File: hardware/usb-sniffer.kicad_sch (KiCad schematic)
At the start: 40 parts, among them IC1 LCMXO2-2000HC, IC2 MIC5504-3.3v, J1 USB-C, J2 USB-C, J3 USB-A, J4 IN, J5 GND

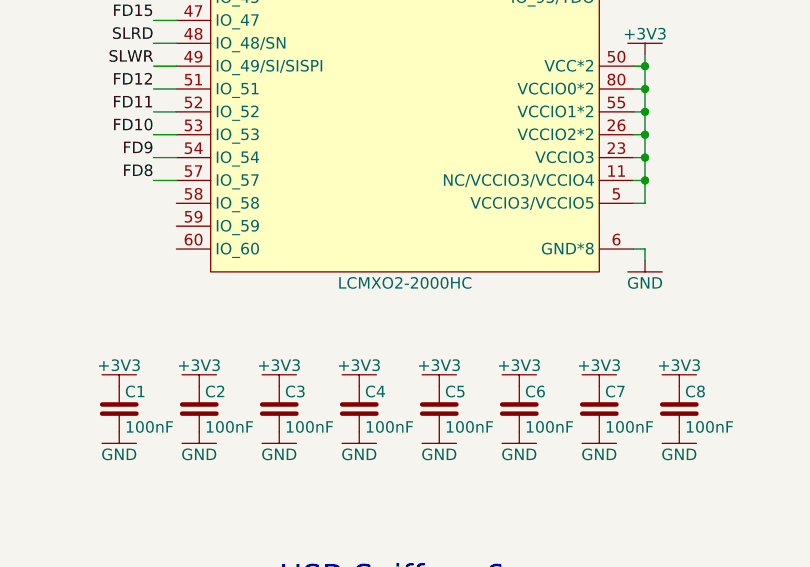
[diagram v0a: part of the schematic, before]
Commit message: Added EEPROM part name
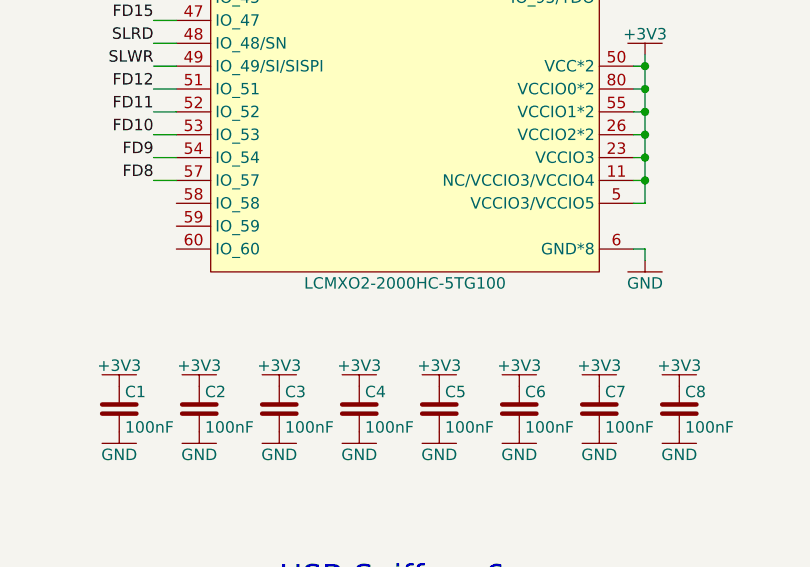
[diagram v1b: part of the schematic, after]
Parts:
- IC1: value LCMXO2-2000HC -> LCMXO2-2000HC-5TG100
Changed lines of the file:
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@@
   (paper "USLetter")
   (title_block
-    (date "2023-05-06")
+    (date "2023-06-16")
     (rev "6")
   )
@@
       (effects (font (size 1.27 1.27)))
     )
-    (property "Value" "LCMXO2-2000HC" (at 146.05 149.86 0)
+    (property "Value" "LCMXO2-2000HC-5TG100" (at 146.05 149.86 0)
       (effects (font (size 1.27 1.27)))
     )

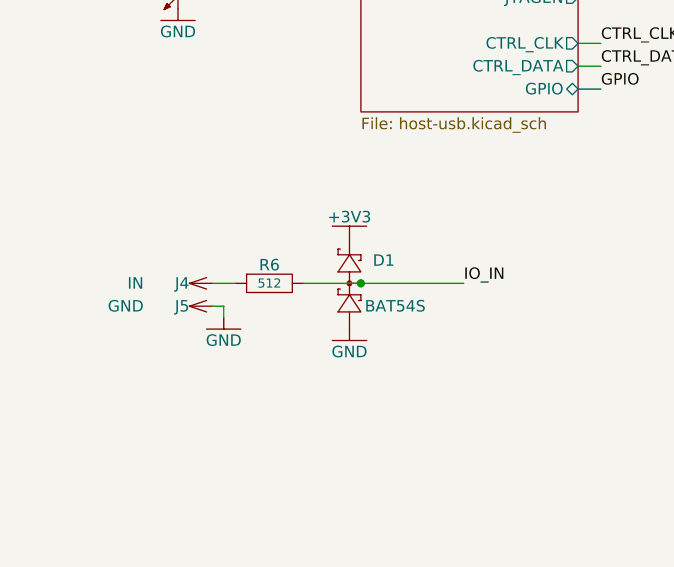
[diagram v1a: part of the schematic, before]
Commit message: Fixed resistor value
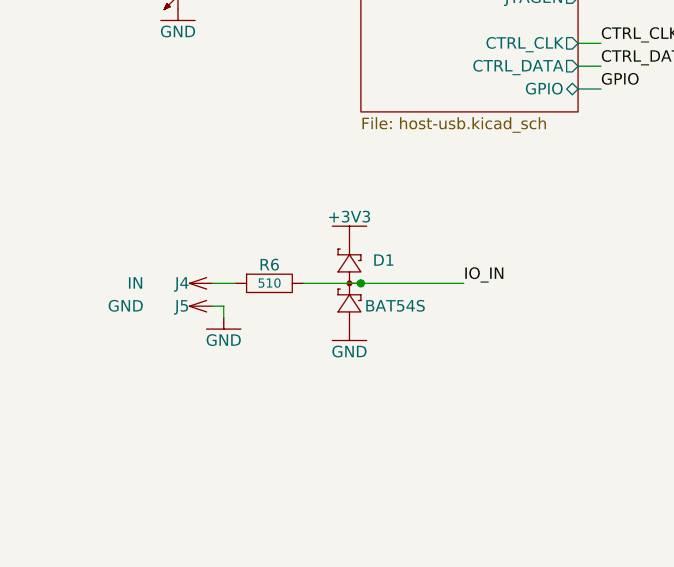
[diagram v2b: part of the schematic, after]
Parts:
- R6: value 512 -> 510
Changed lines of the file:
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@@
       (effects (font (size 1.27 1.27)))
     )
-    (property "Value" "512" (at 41.91 132.08 0)
+    (property "Value" "510" (at 41.91 132.08 0)
       (effects (font (size 1.016 1.016)))
     )
